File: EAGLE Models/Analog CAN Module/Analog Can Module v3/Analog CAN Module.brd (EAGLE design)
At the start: 103.3 x 85.1 mm, 256 parts, among them IC1 AT90CAN128, IC2 MCP2551SO8, IC3 NUP2105L, IC5 FT232RL, Q1 56P2859, U1 LTC2053, U10 LTC2053, U11 LTC2053, U12 LTC2053, U13 LTC2053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

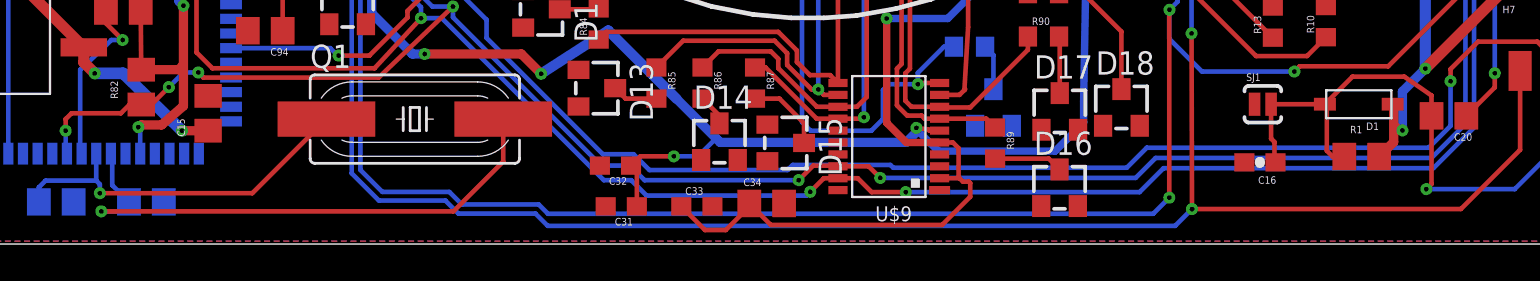
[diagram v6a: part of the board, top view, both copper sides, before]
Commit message: Connected Reset airwire
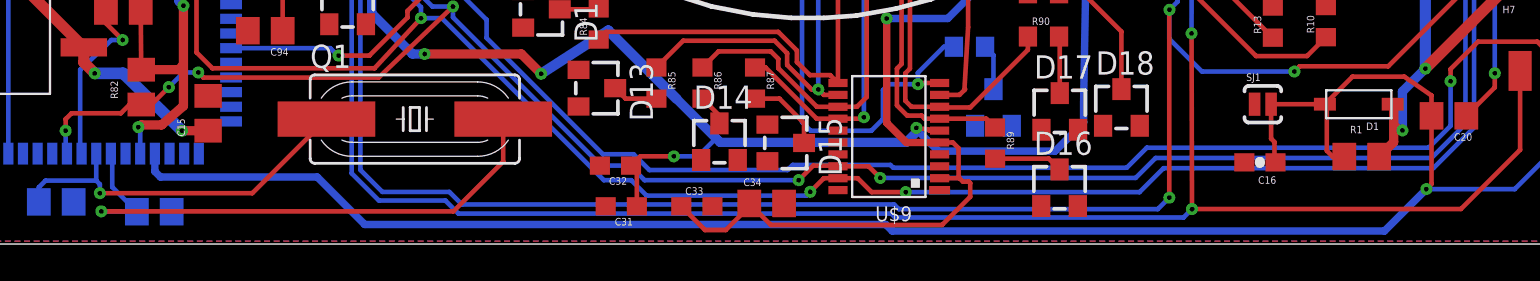
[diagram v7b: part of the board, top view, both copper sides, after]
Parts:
- moved C2 0.69 mm to (19.3, 1.77)
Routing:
- net RESET: track 35.4 -> 108.1 mm
- net XTAL1: track 30.2 -> 31.1 mm
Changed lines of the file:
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@@
 <layer number="27" name="tValues" color="7" fill="1" visible="yes" active="yes"/>
 <layer number="28" name="bValues" color="7" fill="1" visible="yes" active="yes"/>
-<layer number="29" name="tStop" color="7" fill="3" visible="no" active="yes"/>
-<layer number="30" name="bStop" color="7" fill="6" visible="no" active="yes"/>
-<layer number="31" name="tCream" color="7" fill="4" visible="no" active="yes"/>
-<layer number="32" name="bCream" color="7" fill="5" visible="no" active="yes"/>
-<layer number="33" name="tFinish" color="6" fill="3" visible="no" active="yes"/>
-<layer number="34" name="bFinish" color="6" fill="6" visible="no" active="yes"/>
-<layer number="35" name="tGlue" color="7" fill="4" visible="no" active="yes"/>
-<layer number="36" name="bGlue" color="7" fill="5" visible="no" active="yes"/>
+<layer number="29" name="tStop" color="7" fill="3" visible="yes" active="yes"/>
+<layer number="30" name="bStop" color="7" fill="6" visible="yes" active="yes"/>
+<layer number="31" name="tCream" color="7" fill="4" visible="yes" active="yes"/>
+<layer number="32" name="bCream" color="7" fill="5" visible="yes" active="yes"/>
+<layer number="33" name="tFinish" color="6" fill="3" visible="yes" active="yes"/>
+<layer number="34" name="bFinish" color="6" fill="6" visible="yes" active="yes"/>
+<layer number="35" name="tGlue" color="7" fill="4" visible="yes" active="yes"/>
+<layer number="36" name="bGlue" color="7" fill="5" visible="yes" active="yes"/>
 <layer number="37" name="tTest" color="7" fill="1" visible="yes" active="yes"/>
 <layer number="38" name="bTest" color="7" fill="1" visible="yes" active="yes"/>
@@
 <element name="C18" library="rcl" package="C0805" value="100n" x="97.22485" y="47.3964" rot="R90"/>
 <element name="C19" library="rcl" package="C0805" value="100n" x="94.5261" y="46.7614" rot="R90"/>
-<element name="C2" library="rcl" package="C0805" value="18pF" x="18.86585" y="2.2987" rot="MR0"/>
+<element name="C2" library="rcl" package="C0805" value="18pF" x="19.29765" y="1.7653" rot="MR0"/>
 <element name="C20" library="rcl" package="C0805" value="100n" x="89.9795" y="6.9977" rot="R180"/>
 <element name="C21" library="rcl" package="C0603" value="0.1uF" x="36.1061" y="56.6039" rot="MR90"/>
@@
 <via x="16.405225" y="1.7827625" extent="1-16" drill="0.254" diameter="0.508"/>
 <wire x1="35.6282625" y1="1.7827625" x2="16.405225" y2="1.7827625" width="0.254" layer="1"/>
-<wire x1="17.00145" y1="4.86145" x2="17.00145" y2="3.2131" width="0.254" layer="16"/>
-<wire x1="17.00145" y1="3.2131" x2="17.91585" y2="2.2987" width="0.254" layer="16"/>
-<wire x1="17.91585" y1="2.2987" x2="17.3999125" y2="1.7827625" width="0.254" layer="16"/>
+<wire x1="17.00145" y1="4.86145" x2="17.00145" y2="3.1115" width="0.254" layer="16"/>
+<wire x1="18.34765" y1="1.7653" x2="17.3999125" y2="1.7827625" width="0.254" layer="16"/>
 <wire x1="17.3999125" y1="1.7827625" x2="16.405225" y2="1.7827625" width="0.254" layer="16"/>
+<wire x1="17.00145" y1="3.1115" x2="18.34765" y2="1.7653" width="0.254" layer="16"/>
 </signal>
 <signal name="RESET">
@@
 <wire x1="87.5411" y1="9.13765" x2="84.7132" y2="9.13765" width="0.254" layer="1"/>
 <wire x1="84.7132" y1="9.13765" x2="83.20825" y2="7.6327" width="0.254" layer="1"/>
-<wire x1="19.32895" y1="4.93395" x2="80.2695" y2="5.75395" width="0" layer="19" extent="1-16"/>
+<wire x1="19.32895" y1="4.93395" x2="19.32895" y2="3.96285" width="0.4064" layer="16"/>
+<wire x1="19.32895" y1="3.96285" x2="19.6342" y2="3.6576" width="0.4064" layer="16"/>
+<wire x1="19.6342" y1="3.6576" x2="28.194" y2="3.6576" width="0.4064" layer="16"/>
+<wire x1="28.194" y1="3.6576" x2="30.7848" y2="1.0668" width="0.4064" layer="16"/>
+<wire x1="30.7848" y1="1.0668" x2="59.2328" y2="1.0668" width="0.4064" layer="16"/>
+<wire x1="59.2328" y1="1.0668" x2="59.5884" y2="0.7112" width="0.4064" layer="16"/>
+<wire x1="59.5884" y1="0.7112" x2="86.4616" y2="0.7112" width="0.4064" layer="16"/>
+<wire x1="86.4616" y1="0.7112" x2="88.7476" y2="2.9972" width="0.4064" layer="16"/>
 </signal>
 <signal name="PF0">
@@
 <wire x1="83.7286" y1="35.49015" x2="83.88985" y2="35.6514" width="0.254" layer="1"/>
 <wire x1="35.188525" y1="2.3749" x2="35.9029" y2="1.660525" width="0.254" layer="16"/>
-<wire x1="35.9029" y1="1.660525" x2="40.109775" y2="1.660525" width="0.254" layer="16"/>
-<wire x1="40.109775" y1="1.660525" x2="40.7797" y2="0.9906" width="0.254" layer="16"/>
-<wire x1="40.7797" y1="0.9906" x2="75.0316" y2="0.9906" width="0.254" layer="16"/>
 <wire x1="75.95235" y1="1.91135" x2="75.92695" y2="11.49985" width="0.254" layer="1"/>
-<wire x1="75.95235" y1="1.91135" x2="75.0316" y2="0.9906" width="0.254" layer="16"/>
 <wire x1="30.0736" y1="3.8608" x2="31.5595" y2="2.3749" width="0.254" layer="16"/>
 <wire x1="31.5595" y1="2.3749" x2="35.188525" y2="2.3749" width="0.254" layer="16"/>
@@
 <wire x1="93.8657" y1="5.1435" x2="90.63355" y2="1.91135" width="0.254" layer="1"/>
 <wire x1="90.63355" y1="1.91135" x2="75.95235" y2="1.91135" width="0.254" layer="1"/>
+<wire x1="35.9029" y1="1.660525" x2="59.528075" y2="1.660525" width="0.254" layer="16"/>
+<wire x1="59.528075" y1="1.660525" x2="59.7408" y2="1.4478" width="0.254" layer="16"/>
+<wire x1="59.7408" y1="1.4478" x2="75.4888" y2="1.4478" width="0.254" layer="16"/>
+<wire x1="75.4888" y1="1.4478" x2="75.95235" y2="1.91135" width="0.254" layer="16"/>
 </signal>
 <signal name="RX">
@@
 <wire x1="74.710925" y1="2.530475" x2="74.710925" y2="12.7777875" width="0.254" layer="1"/>
 <wire x1="74.710925" y1="12.7777875" x2="74.7220375" y2="12.7889" width="0.254" layer="1"/>
-<wire x1="73.83145" y1="1.651" x2="74.710925" y2="2.530475" width="0.254" layer="16"/>
 <wire x1="30.54985" y1="14.0589" x2="30.54985" y2="4.04495" width="0.254" layer="16"/>
 <wire x1="30.54985" y1="4.04495" x2="31.75" y2="2.8448" width="0.254" layer="16"/>
 <wire x1="31.75" y1="2.8448" x2="35.4076" y2="2.8448" width="0.254" layer="16"/>
 <wire x1="35.4076" y1="2.8448" x2="36.0934" y2="2.159" width="0.254" layer="16"/>
-<wire x1="36.0934" y1="2.159" x2="40.2844" y2="2.159" width="0.254" layer="16"/>
-<wire x1="40.2844" y1="2.159" x2="40.7924" y2="1.651" width="0.254" layer="16"/>
-<wire x1="40.7924" y1="1.651" x2="73.83145" y2="1.651" width="0.254" layer="16"/>
 <wire x1="23.48865" y1="17.89365" x2="26.7151" y2="17.89365" width="0.254" layer="16"/>
 <wire x1="26.7151" y1="17.89365" x2="30.54985" y2="14.0589" width="0.254" layer="16"/>
@@
 <wire x1="74.710925" y1="11.2014" x2="74.710925" y2="12.7777875" width="0.254" layer="16"/>
 <wire x1="74.710925" y1="12.7777875" x2="74.7220375" y2="12.7889" width="0.254" layer="16"/>
+<wire x1="36.0934" y1="2.159" x2="59.69" y2="2.159" width="0.254" layer="16"/>
+<wire x1="59.69" y1="2.159" x2="59.944" y2="1.905" width="0.254" layer="16"/>
+<wire x1="59.944" y1="1.905" x2="74.08545" y2="1.905" width="0.254" layer="16"/>
+<wire x1="74.08545" y1="1.905" x2="74.710925" y2="2.530475" width="0.254" layer="16"/>
 </signal>
 <signal name="SCL">

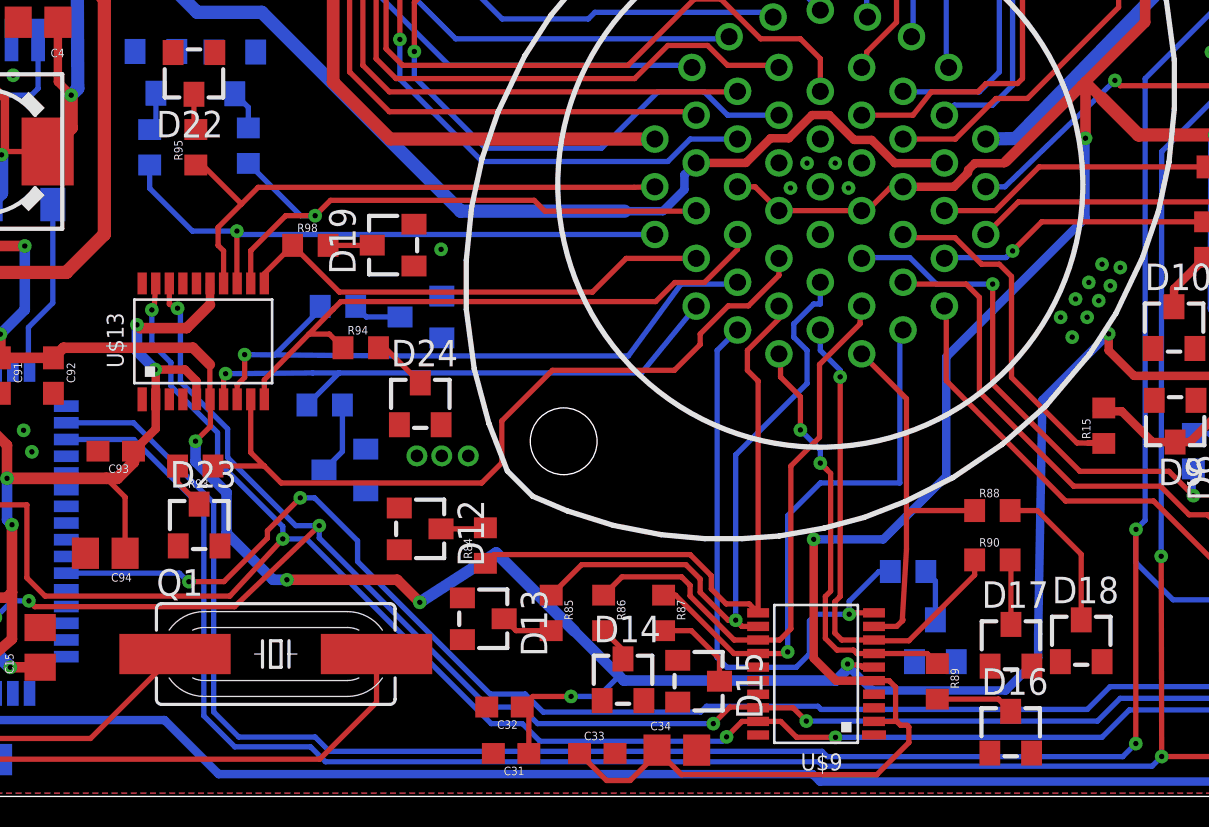
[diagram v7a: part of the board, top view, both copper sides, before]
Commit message: Corrected ADC imputs
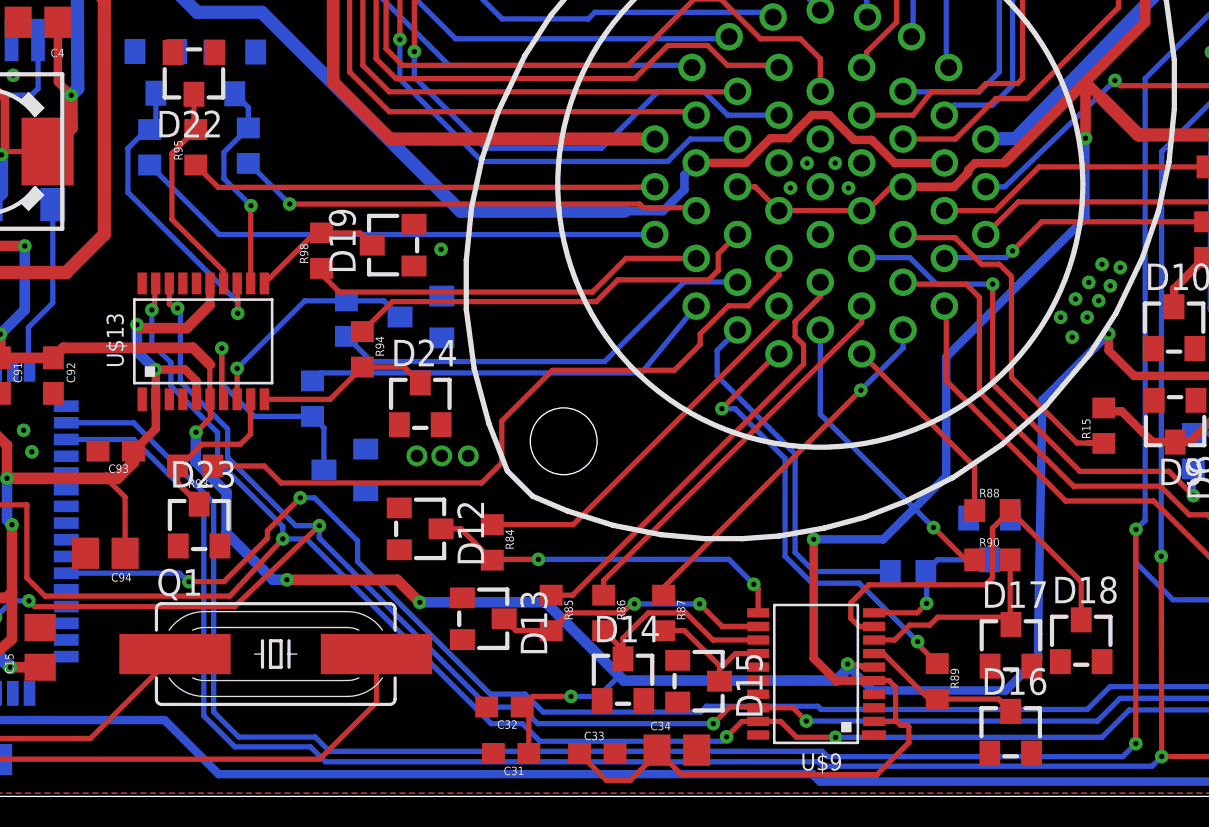
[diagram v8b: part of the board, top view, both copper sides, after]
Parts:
- moved D11 5.52 mm to (67.7, 12.3), turned to 180 degrees
- moved R92 0.71 mm to (36.9, 22.9), turned to 90 degrees
- moved R91 0.66 mm to (35.3, 19.1), turned to 270 degrees
- moved R98 0.59 mm to (35.7, 26.1), turned to 90 degrees
- moved R84 0.36 mm to (43.9, 12.2), turned to 270 degrees
- moved R94 0.11 mm to (37.7, 21.4), turned to 270 degrees
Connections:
- net A10: no longer U$9.8
- net A10CC: now also U$9.8
- net A11: no longer U$9.9
- net A11CC: now also U$9.9
- net A12: no longer U$9.10
- net A12CC: now also U$9.10
- net A13: no longer U$9.11
- net A13CC: now also U$9.11
- net A14: no longer U$9.12
- net A14CC: now also U$9.12
- net A15: no longer U$9.13
- net A15CC: now also U$9.13
- net A16: no longer U$9.14
- net A16CC: now also U$9.14
- net A17: no longer U$13.7
- net A17CC: now also U$13.7
- net A18: no longer U$13.8
- net A18CC: now also U$13.8
- net A19: no longer U$13.9
- net A19CC: now also U$13.9
- net A20: no longer U$13.10
- net A20CC: now also U$13.10
- net A21: no longer U$13.11
- net A21CC: now also U$13.11
- net A22: no longer U$13.12
- net A22CC: now also U$13.12
- net A23: no longer U$13.13
- net A23CC: now also U$13.13
- net A24: no longer U$13.14
- net A24CC: now also U$13.14
- net A9: no longer U$9.7
- net A9CC: now also U$9.7
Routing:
- net A13CC: track 2.14 -> 17.7 mm, vias 0 -> 2
- net A23CC: track 1.86 -> 14.8 mm, vias 0 -> 1
- net A11CC: track 7.41 -> 19.5 mm
- net A13: track 30.4 -> 18.5 mm
- net A12: track 29.0 -> 17.5 mm, vias 1 -> 0
- net A14CC: track 2.49 -> 13.4 mm, vias 0 -> 2
- net A18: track 30.9 -> 20.8 mm, vias 1 -> 0
- net A16: track 27.1 -> 17.5 mm
- net A10: track 23.9 -> 14.3 mm
- net A14: track 30.7 -> 21.3 mm, vias 1 -> 0
- net A15: track 28.0 -> 19.0 mm
- net A24CC: track 1.72 -> 10.6 mm
- net A11: track 18.6 -> 9.75 mm
- net A18CC: track 2.34 -> 10.9 mm, vias 0 -> 1
- net A15CC: track 1.73 -> 10.2 mm
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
